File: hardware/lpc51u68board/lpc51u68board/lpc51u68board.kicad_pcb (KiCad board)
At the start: 2 copper layers, 68.6 x 53.3 mm, 8 parts, among them P1 Power, P2 Analog, P3 Digital, P4 Digital, P5 CONN_01X01, P6 CONN_01X01, P7 CONN_01X01, P8 CONN_01X01

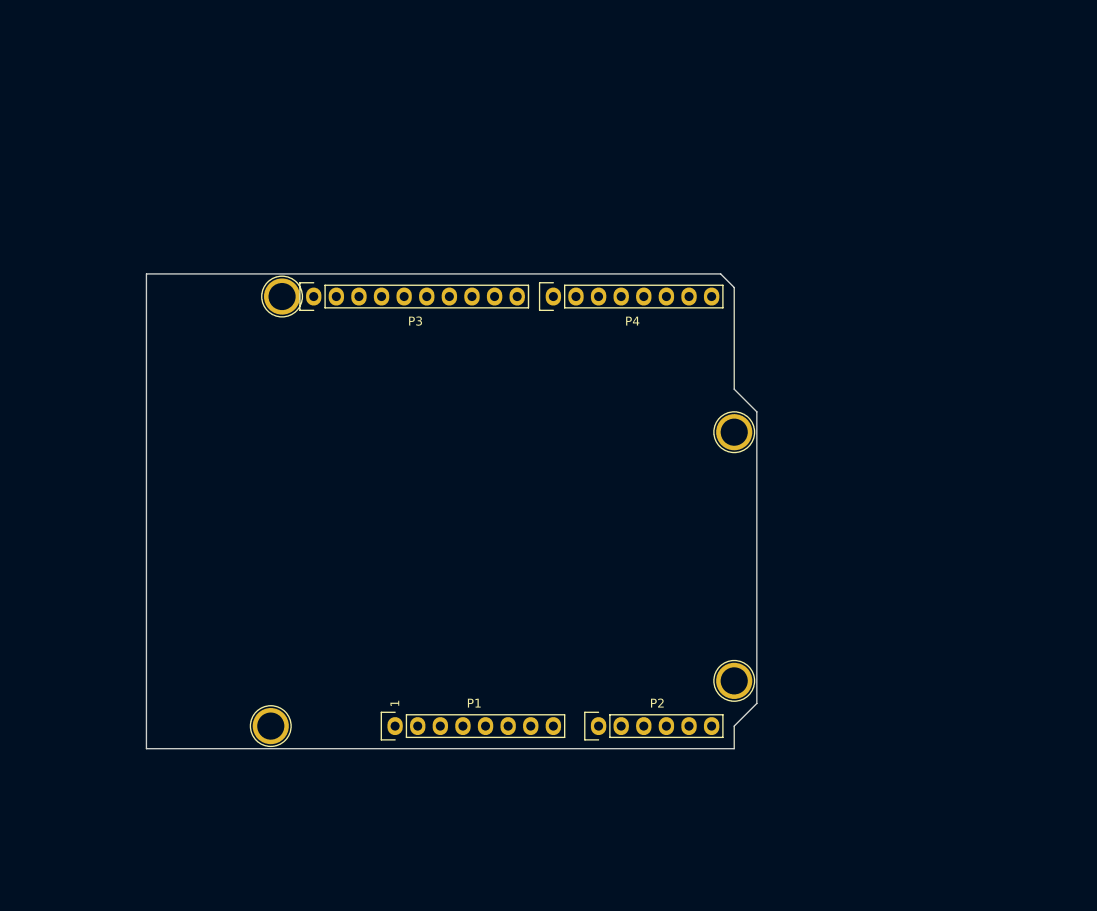
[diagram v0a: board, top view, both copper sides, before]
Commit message: NXP LPC51u68 layout I
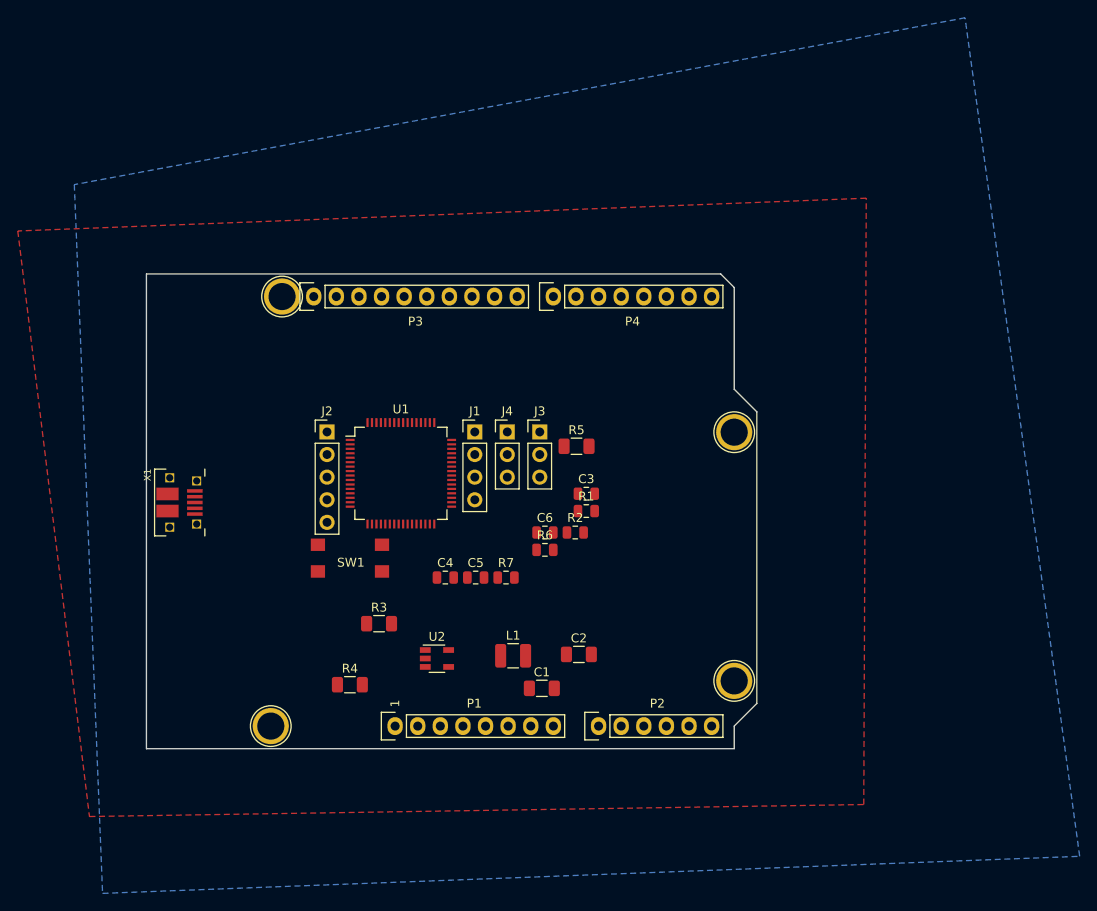
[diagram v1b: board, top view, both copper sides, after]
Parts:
- added C1: 4.7uF, Capacitor_SMD:C_1206_3216Metric, F.Cu at (155.4, 119.6)
- added C2: 10uF, Capacitor_SMD:C_1206_3216Metric, F.Cu at (159.6, 115.8)
- added C3: 0.1uF, Capacitor_SMD:C_0805_2012Metric, F.Cu at (160.4, 97.7)
- added C4: 0.1uF, Capacitor_SMD:C_0805_2012Metric, F.Cu at (144.6, 107.1)
- added C5: 0.1uF, Capacitor_SMD:C_0805_2012Metric, F.Cu at (148.0, 107.1)
- added C6: 0.1uF, Capacitor_SMD:C_0805_2012Metric, F.Cu at (155.8, 102.1)
- added J1: VBUS_Sel, Connector_PinHeader_2.54mm:PinHeader_1x04_P2.54mm_Vertical, F.Cu at (147.9, 90.8)
- added J2: Conn_01x05_Male, Connector_PinHeader_2.54mm:PinHeader_1x05_P2.54mm_Vertical, F.Cu at (131.3, 90.8)
- added J3: ISP0_Sel, Connector_PinHeader_2.54mm:PinHeader_1x03_P2.54mm_Vertical, F.Cu at (155.2, 90.8)
- added J4: ISP1_Sel, Connector_PinHeader_2.54mm:PinHeader_1x03_P2.54mm_Vertical, F.Cu at (151.5, 90.8)
- added L1: 2.2uH, Inductor_SMD:L_1210_3225Metric, F.Cu at (152.2, 115.9)
- added R1: 33 ohm, Resistor_SMD:R_0805_2012Metric, F.Cu at (160.4, 99.7)
- added R2: 33 ohm, Resistor_SMD:R_0805_2012Metric, F.Cu at (159.2, 102.1)
- added R3: 450kohm, Resistor_SMD:R_1206_3216Metric, F.Cu at (137.1, 112.3)
- added R4: 100kohm, Resistor_SMD:R_1206_3216Metric, F.Cu at (133.9, 119.2)
- added R5: 100kohm, Resistor_SMD:R_1206_3216Metric, F.Cu at (159.3, 92.4)
- added R6: 2.2kohm, Resistor_SMD:R_0805_2012Metric, F.Cu at (155.8, 104.0)
- added R7: 2.2kohm, Resistor_SMD:R_0805_2012Metric, F.Cu at (151.4, 107.1)
- added SW1: TL3305CF260QG, kifootp:TL3305-C, F.Cu at (133.9, 105.0)
- added U1: LPC51u68, Package_QFP:LQFP-64_10x10mm_P0.5mm, F.Cu at (139.6, 95.4)
- added U2: LTC3406ES5, Package_TO_SOT_SMD:TSOT-23-5, F.Cu at (143.6, 116.2)
- added X1: USBFCI_10103594, kifootp:FCI_10103594_MILL, F.Cu at (111.9, 98.7)
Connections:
- P1 pad 8: /Vin -> +5V
- P2 pad 5: /A4(SDA) -> /A4
- P2 pad 6: /A5(SCL) -> /A5
- P5 pad 1: Net-(P5-Pad1) -> GND
- P6 pad 1: Net-(P6-Pad1) -> GND
- P7 pad 1: Net-(P7-Pad1) -> GND
- P8 pad 1: Net-(P8-Pad1) -> GND
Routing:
- added copper zone on B.Cu, net GND
- added copper zone on F.Cu, net GND

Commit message: NXP LPC51u68 layout II
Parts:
- added R8: 100kohm, Resistor_SMD:R_1206_3216Metric, F.Cu at (117.6, 89.3)
- added R9: 100kohm, Resistor_SMD:R_1206_3216Metric, F.Cu at (115.5, 84.8)
- J2: value Conn_01x05_Male -> SWD
- moved R1 33.9 mm to (126.6, 99.8), turned to 180 degrees
- moved R2 33.0 mm to (126.5, 97.5), turned to 180 degrees
- moved C6 23.9 mm to (131.9, 101.9)
- moved R6 23.9 mm to (131.9, 103.9)
- moved J1 21.7 mm to (168.3, 98.0)
- moved C4 17.0 mm to (127.9, 110.6)
- moved C5 17.0 mm to (131.4, 110.6)
- moved R7 17.0 mm to (134.8, 110.6)
- moved SW1 17.0 mm to (117.2, 108.4)
- moved C3 13.0 mm to (169.3, 88.2)
- moved J3 13.0 mm to (164.1, 81.2)
- moved J4 13.0 mm to (160.4, 81.2)
- moved R5 13.0 mm to (168.2, 82.8)
- moved J2 10.7 mm to (122.8, 84.3)
- moved U1 8.25 mm to (147.1, 98.9), turned to 315 degrees
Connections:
- U1 pad 5: Net-(R2-Pad1) -> Net-(R1-Pad1)
- U1 pad 6: Net-(R1-Pad1) -> Net-(R2-Pad1)
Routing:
- net /13(SCK): track 0.00 -> 37.5 mm
- net /11(**/MOSI): track 0.00 -> 35.3 mm
- net /12(MISO): track 0.00 -> 34.4 mm
- net /10(**/SS): track 0.00 -> 25.4 mm, vias 0 -> 1
- net /A4(SDA): track 0.00 -> 24.3 mm
- net /A5(SCL): track 0.00 -> 23.3 mm
- net Net-(R1-Pad1): track 0.00 -> 20.4 mm
- net Net-(R2-Pad1): track 0.00 -> 19.1 mm
- net Net-(R1-Pad2): track 0.00 -> 9.52 mm
- net Net-(R2-Pad2): track 0.00 -> 8.49 mm
- net GND: vias 0 -> 3

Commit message: NXP LPC51u68 layout III
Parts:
- moved SW1 52.1 mm to (164.3, 86.1)
- moved J3 32.1 mm to (166.9, 113.2)
- moved R7 28.3 mm to (141.8, 83.2), turned to 180 degrees
- moved C5 20.4 mm to (151.5, 107.3)
- moved C3 19.7 mm to (149.6, 88.5)
- moved C2 19.0 mm to (141.0, 119.7)
- moved R6 18.3 mm to (135.5, 85.9), turned to 90 degrees
- moved L1 16.4 mm to (136.0, 118.7), turned to 90 degrees
- moved R4 15.0 mm to (147.4, 112.8)
- moved C4 13.1 mm to (139.8, 105.1)
- moved C6 11.7 mm to (139.3, 92.8), turned to 180 degrees
- moved J4 11.2 mm to (160.1, 92.5)
- moved C1 9.04 mm to (146.4, 119.7), turned to 180 degrees
- moved R5 8.45 mm to (165.2, 90.7)
- moved R3 4.24 mm to (141.3, 112.9)
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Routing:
- net +3V3: track 0.00 -> 205.2 mm, vias 0 -> 9
- net /Reset: track 0.00 -> 92.5 mm, vias 0 -> 7
- net +5V: track 0.00 -> 92.0 mm, vias 0 -> 3
- net /0(Rx): track 0.00 -> 56.8 mm
- net /1(Tx): track 0.00 -> 56.4 mm
- net /A2: track 0.00 -> 54.1 mm, vias 0 -> 3
- net /A3: track 0.00 -> 48.9 mm, vias 0 -> 3
- net /A4: track 0.00 -> 48.7 mm, vias 0 -> 3
- net /A1: track 0.00 -> 45.9 mm, vias 0 -> 3
- net /A0: track 0.00 -> 40.2 mm, vias 0 -> 1
- net Net-(J2-Pad2): track 0.00 -> 38.9 mm, vias 0 -> 1
- net Net-(J2-Pad1): track 0.00 -> 38.4 mm, vias 0 -> 1
- net Net-(J2-Pad3): track 0.00 -> 36.9 mm, vias 0 -> 1
- net /A5: track 0.00 -> 34.2 mm, vias 0 -> 3
- net Net-(J1-Pad4): track 0.00 -> 31.5 mm, vias 0 -> 1
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
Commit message: NXP LPC51u68 gerbers I
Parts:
- moved C6 3.15 mm to (136.1, 93.1)
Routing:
- net /A5: track 34.2 -> 49.3 mm
- net +5V: track 92.0 -> 102.0 mm
- net +3V3: track 205.2 -> 210.8 mm
- net GND: track 19.0 -> 23.5 mm, vias 73 -> 75
- net /0(Rx): track 56.8 -> 59.4 mm
- net Net-(J4-Pad3): track 13.3 -> 14.1 mm
